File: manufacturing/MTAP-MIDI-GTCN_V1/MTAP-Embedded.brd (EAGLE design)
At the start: 31.8 x 54.6 mm, 51 parts, among them J1 629105150521, X1 0R, X2 0R

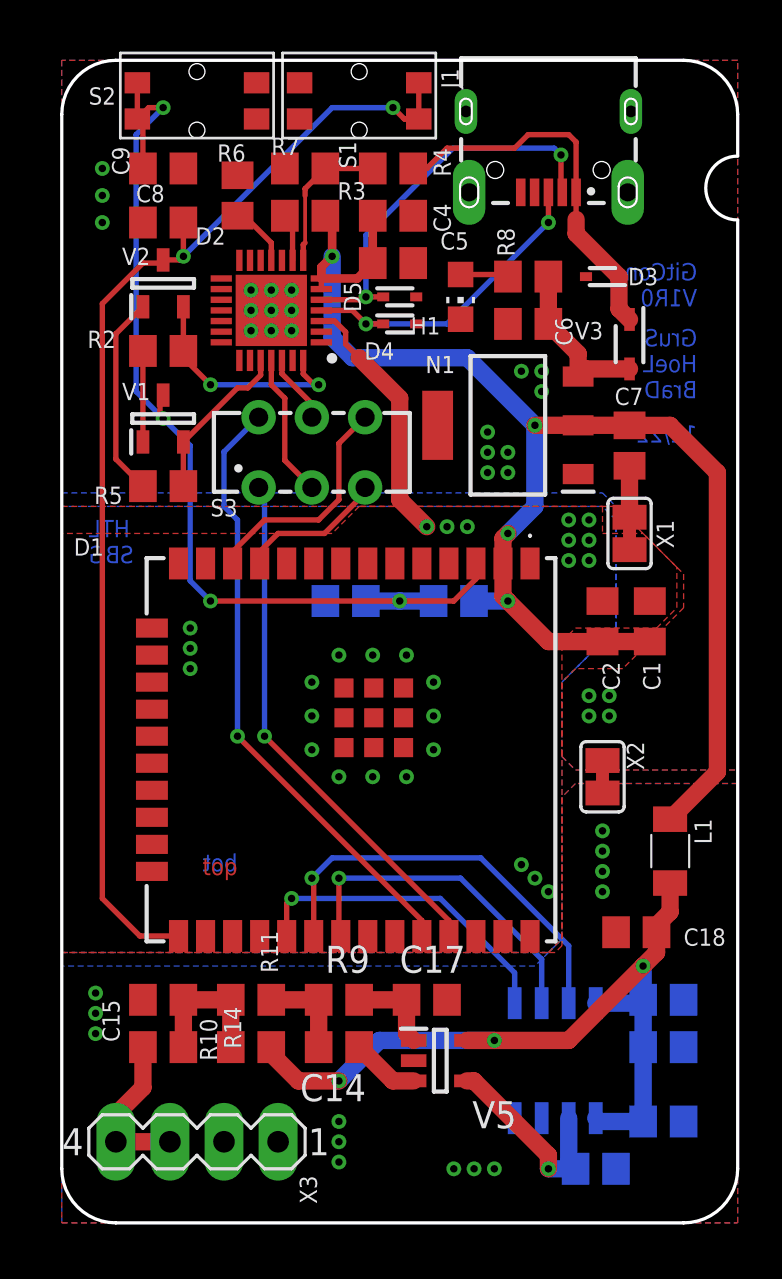
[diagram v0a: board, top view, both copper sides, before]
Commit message: Finished PCB
- Added Test Terminals
- Finalised Filter Design
- Added all 3d models and created external Fusion 360 Project
- Updated Filter simulation draft
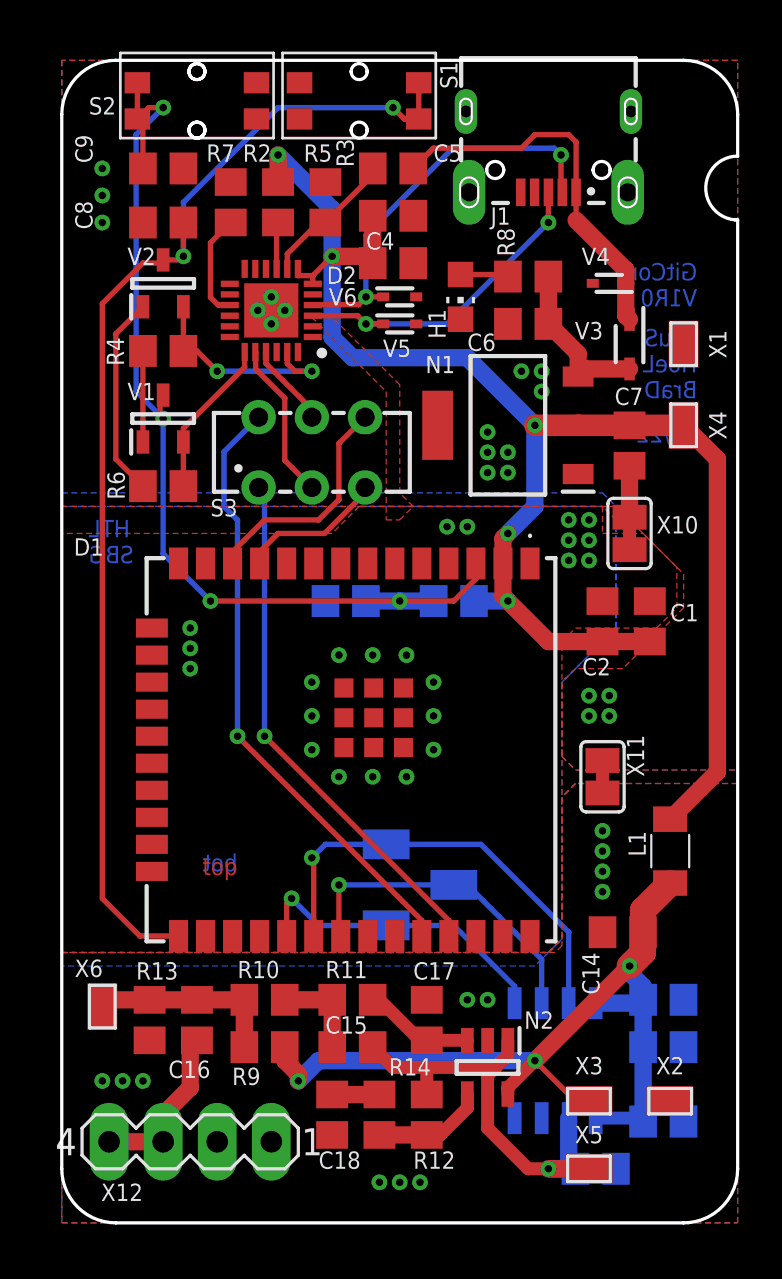
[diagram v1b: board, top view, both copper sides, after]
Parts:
- removed D4: LESD5D5.0CT1G, diode_GruS:SOD523
- removed D6: MCP3201-CI_SN, adc-dac_GruS:SOIC127P600X175-8N
- added C16: 2u2, rcl_GruS:C0805
- added N2: TLV271G4, opv_GruS:SOT95P280X145-5N
- added R12: 22k, rcl_GruS:R0805
- added R13: 10k, rcl_GruS:R0805
- added V4: ESD5B5.0ST1G, diode_GruS:SOD523
- added X10, X11: 0R, con_GruS:MYLIB_SJ-SHORT
- added X12: (no value), con-lstb:MA04-1
- added X4, X5, X6, X7, X8, X9: SMD-TP, solpad_GruS:S2751-46R
- C1, C6, C7: value 22u/10V -> 22u
- C15: value 100n -> 12n
- C17: value 10n -> 6n8
- C18: value 100n -> 2u2
- C2, C3: value 100n/50V -> 100n
- D2: value CP2102N-A01-GQFN28 -> CP2102N; device ic_GruS:QFN28 -> ic_GruS:QFN24
- D3: value LESD5D5.0CT1G -> MCP3201; device diode_GruS:SOD523 -> adc-dac_GruS:SOIC127P600X175-8N
- J1: value 629105150521 -> (none)
- R10: value 10k -> 5k6
- R11: value 12k -> 33k
- R2: value 10k -> 2k
- R3: value 2k -> 22k1
- R4: value 22k1 -> 10k
- R5: value 10k -> 47k5
- R7: value 47k5 -> 10k
- R9: value 12k -> 10k
- S1: value (none) -> BOOT
- S2: value (none) -> EN
- V5: value TLV9151DBV -> ESD5B5.0ST1G; device opv_GruS:SOT95P280X145-5N -> diode_GruS:SOD523
- V6: value LESD5D5.0CT1G -> ESD5B5.0ST1G
- X1, X2: value 0R -> SMD-TP; device con_GruS:MYLIB_SJ-SHORT -> solpad_GruS:S2751-46R
- X3: value (none) -> SMD-TP; device con-lstb:MA04-1 -> solpad_GruS:S2751-46R
- moved D3 36.9 mm to (23.2, 7.62), flipped to the bottom, turned to 90 degrees
- moved V5 34.7 mm to (15.9, 42.2)
- moved X3 18.5 mm to (24.8, 5.71), turned to 0 degrees
- moved C18 16.7 mm to (12.7, 5.08), turned to 270 degrees
- moved X2 15.6 mm to (28.6, 5.71), turned to 180 degrees
- moved R5 15.4 mm to (12.4, 47.9), turned to 270 degrees
- moved C14 14.4 mm to (26.4, 13.7)
- moved R6 14.1 mm to (4.76, 34.6), turned to 180 degrees
- moved R4 13.8 mm to (4.76, 41.0)
- moved R14 11.5 mm to (14.9, 5.08), turned to 270 degrees
- moved X1 9.25 mm to (29.2, 41.3), turned to 90 degrees
- moved C15 8.89 mm to (13.7, 8.26)
- moved R2 8.83 mm to (10.2, 47.9), turned to 270 degrees
- moved R11 4.76 mm to (13.7, 10.5)
- moved R3 4.69 mm to (15.6, 49.5)
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- renumbered D5 to V6
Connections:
- removed net N$17: C15.2, X3.3, X3.4
- removed net N$8: C15.1, R10.1, R11.1, R14.2
- new net IN0: C16.2, X12.3, X12.4
- new net IN1: C16.1, R10.1, R13.2, R9.1, X6.P$1
- new net N$5: D2.15, R7.2
- new net N$9: D2.9, R2.2
- net +3V3: now also R2.1, X4.P$1; no longer R3.1
- net AGND: now also C14.2, D3.3, D3.4, N2.2, R13.1, X11.2, X12.1, X12.2, X2.P$1; no longer D6.3, D6.4, R14.1, V5.2, X2.2, X3.1, X3.2
- net AINP: now also C15.1, D3.2, N2.1, R12.2, X5.P$1; no longer C14.1, D6.2, V5.3, V5.4
- net AVDD: now also C14.1, D3.1, D3.8, N2.5, R9.2, X3.P$1; no longer C18.1, D6.1, D6.8, R10.2, V5.5
- net DTR: now also D2.23, R4.1; no longer D2.28, R2.1
- net GND: now also D2.2, X10.2; no longer D2.3, X1.2
- net N$15: now also R4.2; no longer R2.2
- net N$16: now also R6.2; no longer R5.2
- net N$2: now also R3.2, R5.2; no longer R4.2, R7.2
- net N$3: now also N2.4, R12.1, R14.2; no longer D2.11, R6.2
- net N$4: now also C18.1, R14.1; no longer D2.9, R3.2
- net N$6: now also N2.3, R11.2; no longer R9.2, V5.1
- net N$7: now also C15.2, R10.2, R11.1; no longer C14.2, R11.2, R9.1
- net PGND: now also R5.1, V4.2, V5.2, X1.P$1, X10.1, X11.1; no longer D2.29, D3.2, D4.2, R6.1, X1.1, X2.1
- net RTS: now also D2.19, R6.1; no longer D2.24, R5.1
- net RXD: now also D2.20; no longer D2.25
- net TXD: now also D2.21; no longer D2.26
- net USB_DN: now also D2.4; no longer D2.5
- net USB_DP: now also D2.3, V5.1; no longer D2.4, D4.1
- net VBUS: now also R3.1, V4.1; no longer D3.1, R4.1
- net VSPIQ_MISO: now also D3.6, X8.P$1; no longer D6.6
- net VSPI_!CS: now also D3.5, X7.P$1; no longer D6.5
- net VSPI_CLK: now also D3.7, X9.P$1; no longer D6.7
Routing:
- net GND: track 12.1 -> 0.00 mm, vias 27 -> 23
- net IN1: track 0.00 -> 9.02 mm
- net AINP: track 12.9 -> 21.3 mm
- net IN0: track 0.00 -> 7.96 mm
- net N$17: track 7.51 -> 0.00 mm
- net N$8: track 6.67 -> 0.00 mm
- net +3V3: track 68.5 -> 74.2 mm, vias 4 -> 5
- net N$5: track 0.00 -> 4.97 mm
- net AVDD: track 38.1 -> 42.3 mm
- net N$3: track 2.94 -> 5.31 mm
- net N$9: track 0.00 -> 2.21 mm
- net GPIO0: track 54.4 -> 55.9 mm
- net VSPI_CLK: track 19.6 -> 21.1 mm
- net N$6: track 4.27 -> 5.25 mm
- net TXD: track 3.25 -> 3.96 mm
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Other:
- outline, holes or cut-outs redrawn
- board text added: "BOOT"
- board text added: "RST"

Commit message: upd STL
added Reference for docs
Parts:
- R4, R6: value 10k -> 12k
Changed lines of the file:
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@@
 <attribute name="VALUE" x="22.225" y="45.4025" size="0.8128" layer="27" font="vector" ratio="12" rot="R90"/>
 </element>
-<element name="R4" library="rcl_GruS" library_urn="urn:adsk.eagle:library:13572313" package="R0805" package3d_urn="urn:adsk.eagle:package:18365371/1" value="10k" x="4.7625" y="40.9575" smashed="yes" rot="R180">
+<element name="R4" library="rcl_GruS" library_urn="urn:adsk.eagle:library:13572313" package="R0805" package3d_urn="urn:adsk.eagle:package:18365371/1" value="12k" x="4.7625" y="40.9575" smashed="yes" rot="R180">
 <attribute name="NAME" x="2.921" y="40.259" size="0.8128" layer="25" font="vector" ratio="12" rot="R90"/>
 <attribute name="VALUE" x="7.1755" y="40.4495" size="0.8128" layer="27" font="vector" ratio="12" rot="R90"/>
 </element>
-<element name="R6" library="rcl_GruS" library_urn="urn:adsk.eagle:library:13572313" package="R0805" package3d_urn="urn:adsk.eagle:package:18365371/1" value="10k" x="4.7625" y="34.6075" smashed="yes" rot="R180">
+<element name="R6" library="rcl_GruS" library_urn="urn:adsk.eagle:library:13572313" package="R0805" package3d_urn="urn:adsk.eagle:package:18365371/1" value="12k" x="4.7625" y="34.6075" smashed="yes" rot="R180">
 <attribute name="NAME" x="2.9591" y="33.9725" size="0.8128" layer="25" font="vector" ratio="12" rot="R90"/>
 <attribute name="VALUE" x="3.2385" y="33.0835" size="0.8128" layer="27" font="vector" ratio="12"/>

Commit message: upd schematic
home office push
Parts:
- renumbered X1 to PGND, X2 to AGND, X3 to AVDD, X4 to 3V3, X5 to POST-AFE, X6 to AIN, X7 to SPI_CS, X8 to SPIQ, X9 to SPI_CLK
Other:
- outline, holes or cut-outs redrawn

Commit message: upd logo and poster
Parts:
- R14: value 10k -> 12k
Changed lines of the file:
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@@
 <setting verticaltext="up"/>
 </settings>
-<grid distance="0.25" unitdist="mm" unit="mm" style="lines" multiple="1" display="yes" altdistance="0.000123031496" altunitdist="mil" altunit="mil"/>
+<grid distance="25" unitdist="mil" unit="mil" style="lines" multiple="1" display="yes" altdistance="0.000123031496" altunitdist="mil" altunit="mil"/>
 <layers>
 <layer number="1" name="Top" color="4" fill="1" visible="no" active="yes"/>
@@
 </layers>
 <board>
-<fusionsync huburn="a.YnVzaW5lc3M6aHRsc2FsemJ1cmc3OA" projecturn="a.YnVzaW5lc3M6aHRsc2FsemJ1cmc3OCNEMjAxOTEwMTAyMjUyNjg2MjY" f3durn="urn:adsk.wipprod:dm.lineage:PaL6rp13RiSVVNLB_ty64g" pcbguid="" lastpulledtime="2022-11-20T01:33:00Z" lastsyncedchangeguid="" latestrevisionid="b698abed-f2bd-4f1f-9f28-b15b9313db53" lastsyncedrevisionid="b698abed-f2bd-4f1f-9f28-b15b9313db53" lastboardhashguid="34ba4092-3bce-b887-5af5-95b666c2da66" lastpushedtime="2022-11-20T17:35:46Z" linktopcb3d="true"/>
+<fusionsync huburn="a.YnVzaW5lc3M6aHRsc2FsemJ1cmc3OA" projecturn="a.YnVzaW5lc3M6aHRsc2FsemJ1cmc3OCNEMjAxOTEwMTAyMjUyNjg2MjY" f3durn="urn:adsk.wipprod:dm.lineage:PaL6rp13RiSVVNLB_ty64g" pcbguid="" lastpulledtime="2022-11-20T01:33:00Z" lastsyncedchangeguid="" latestrevisionid="6d66a595-1d53-4291-b3cb-babf524249c6" lastsyncedrevisionid="6d66a595-1d53-4291-b3cb-babf524249c6" lastboardhashguid="31a65c2e-e5bd-fd00-9356-c060665ae9f2" lastpushedtime="2022-12-07T17:55:57Z" linktopcb3d="true"/>
 <plain>
 <rectangle x1="1.438021875" y1="18.292190625" x2="1.719959375" y2="18.320384375" layer="22" rot="R90"/>
@@
 <attribute name="VALUE" x="12.065" y="1.5875" size="0.8128" layer="27" font="vector" ratio="12"/>
 </element>
-<element name="R14" library="rcl_GruS" library_urn="urn:adsk.eagle:library:13572313" package="R0805" package3d_urn="urn:adsk.eagle:package:18365371/1" value="10k" x="14.9225" y="5.08" smashed="yes" rot="R270">
+<element name="R14" library="rcl_GruS" library_urn="urn:adsk.eagle:library:13572313" package="R0805" package3d_urn="urn:adsk.eagle:package:18365371/1" value="12k" x="14.9225" y="5.08" smashed="yes" rot="R270">
 <attribute name="NAME" x="15.367" y="6.9215" size="0.8128" layer="25" font="vector" ratio="12"/>
 <attribute name="VALUE" x="14.2875" y="2.54" size="0.8128" layer="27" font="vector" ratio="12"/>
@@
 </polygon>
 <polygon width="0.254" layer="16" isolate="0.254" rank="3">
-<vertex x="0" y="12.7"/>
-<vertex x="22.86" y="12.7"/>
+<vertex x="0" y="12.065"/>
+<vertex x="22.225" y="12.065"/>
 <vertex x="23.495" y="13.335"/>
 <vertex x="23.495" y="25.4"/>
@@
 <vertex x="31.75" y="54.61"/>
 <vertex x="0" y="54.61"/>
-<vertex x="0" y="34.29"/>
-<vertex x="25.4" y="34.29"/>
+<vertex x="0" y="34.04"/>
+<vertex x="25.65" y="34.04"/>
 <vertex x="26.035" y="33.655"/>
 <vertex x="26.035" y="27.94"/>

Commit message: upd Brd
- Power Section
- Diff Pairs
PR Ready
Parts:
- moved H1 10.3 mm to (28.9, 45.1), turned to 0 degrees
- moved V6 8.14 mm to (23.5, 46.4), turned to 270 degrees
- moved V5 7.57 mm to (22.2, 46.4), turned to 270 degrees
- moved R8 6.43 mm to (27.9, 42.2), turned to 180 degrees
- moved C6 6.43 mm to (27.9, 40.0), turned to 0 degrees
- moved PGND 6.02 mm to (23.5, 43.2), turned to 180 degrees
- moved V3 4.14 mm to (27.0, 45.4)
- moved POST-AFE 3.93 mm to (21.0, 3.49)
- moved AVDD 3.86 mm to (24.1, 9.53)
- moved AGND 3.81 mm to (28.6, 9.53)
- moved V4 2.42 mm to (24.8, 46.4), turned to 270 degrees
- moved J1 0.63 mm to (22.9, 51.9)
- turned 3V3 to 0 degrees
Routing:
- net VBUS: track 17.8 -> 14.2 mm
- net AVDD: track 41.9 -> 38.6 mm
- net USB_DN: track 19.1 -> 16.4 mm
- net AINP: track 21.3 -> 19.4 mm
- net USB_DP: track 15.4 -> 16.3 mm
- net +5V: track 7.84 -> 7.08 mm
- net +3V3: track 74.2 -> 73.6 mm
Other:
- outline, holes or cut-outs redrawn

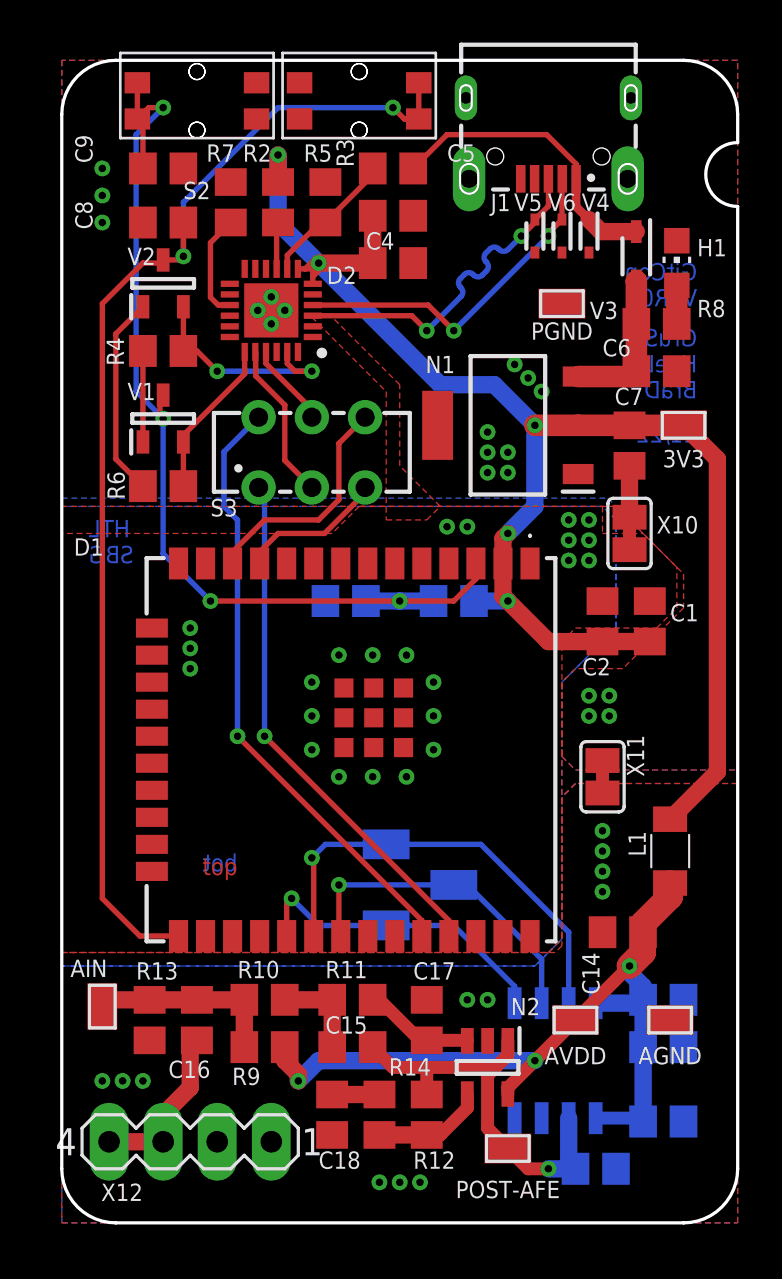
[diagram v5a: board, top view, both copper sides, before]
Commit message: Finalised Board
added missing connections to USB Bridge.
Added 3d Images to docs
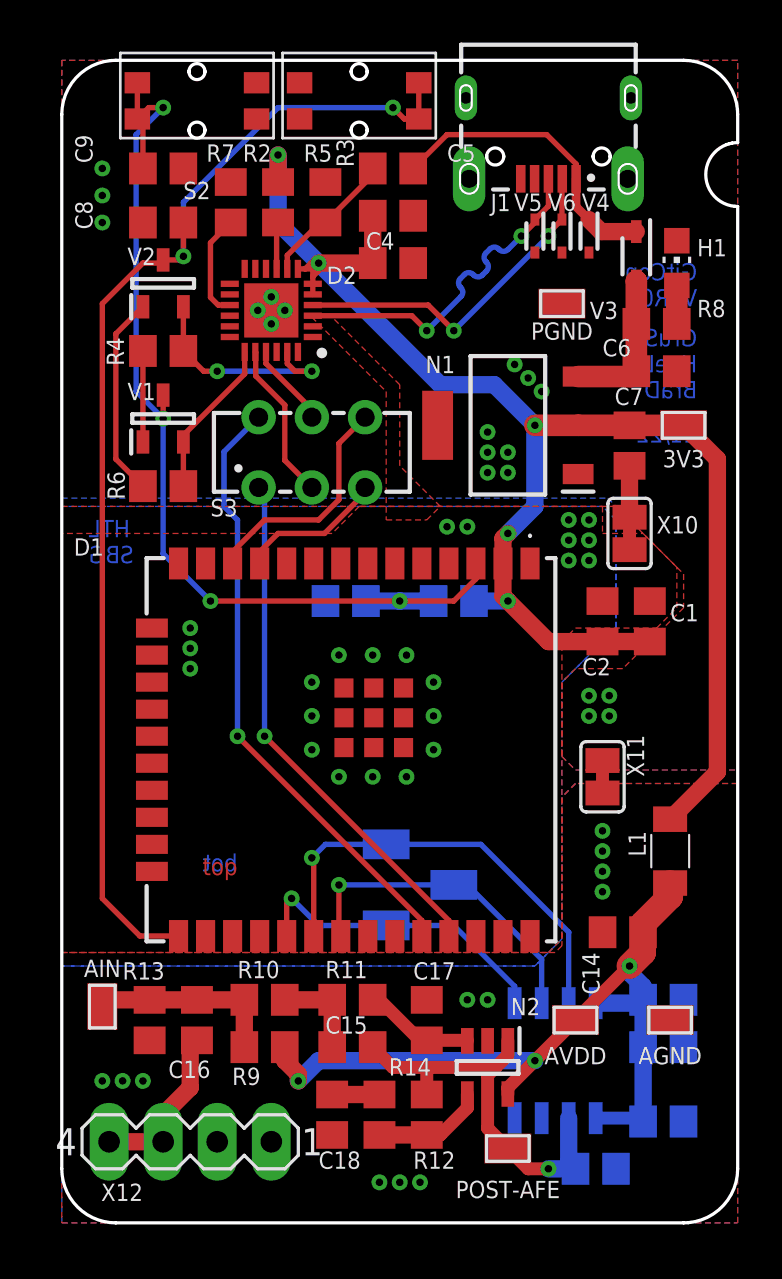
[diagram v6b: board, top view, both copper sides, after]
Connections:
- net +3V3: now also D2.5
- net PGND: now also D2.25
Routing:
- net +3V3: track 73.6 -> 74.1 mm
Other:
- outline, holes or cut-outs redrawn

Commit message: midi functional test
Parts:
- added C19: 1u, rcl_GruS:C0805
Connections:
- net AGND: now also C19.2
- net AINP: now also C19.1, D1.26
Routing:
- net AINP: track 19.4 -> 38.2 mm, vias 1 -> 3
- net AVDD: track 38.6 -> 39.1 mm
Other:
- outline, holes or cut-outs redrawn

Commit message: upd midi serial
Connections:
- new net MTDO: D1.23
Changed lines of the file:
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@@
 <wire x1="12.7" y1="6.03" x2="14.9225" y2="6.03" width="0.8128" layer="1"/>
+</signal>
+<signal name="MTDO">
+<contactref element="D1" pad="23"/>
 </signal>
 </signals>
